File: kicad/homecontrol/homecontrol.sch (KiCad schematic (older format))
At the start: 71 parts, among them J1 Screw_Terminal_01x09, J2 Screw_Terminal_01x09, J3 Screw_Terminal_01x09, J4 Screw_Terminal_01x09, J5 AVR-ISP-10, U1 ATmega48P-20PU, U2 L7805ABP, U3 ULN2803A, U4 MAX232EEPE+, U5 A817, U6 A817

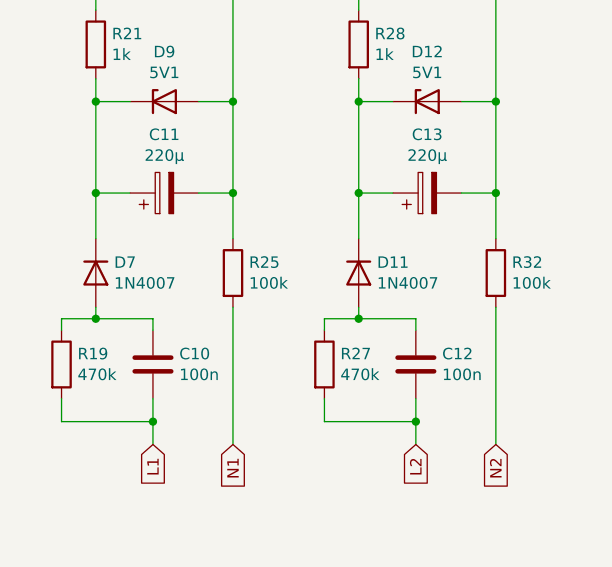
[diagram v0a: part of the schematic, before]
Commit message: Updated footprints and BOM
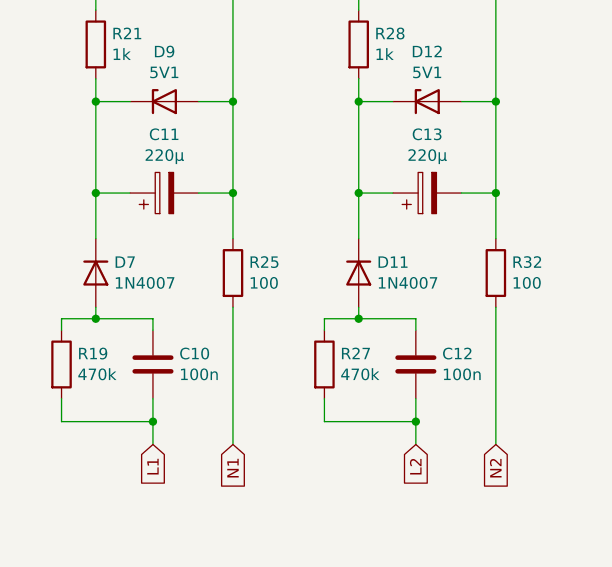
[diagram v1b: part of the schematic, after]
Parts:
- C1, C4: footprint Capacitor_THT:C_Disc_D6.0mm_W2.5mm_P5.00mm -> Capacitor_THT:C_Rect_L7.0mm_W2.5mm_P5.00mm; Supplier (none) -> Digikey; Supplier_Ref (none) -> BC1101CT-ND; Voltage 16V -> 50V
- C10: footprint Capacitor_THT:C_Rect_L10.3mm_W4.5mm_P7.50mm_MKS4 -> Capacitor_THT:C_Rect_L13.0mm_W4.0mm_P10.00mm_FKS3_FKP3_MKS4
- C11, C13: footprint Capacitor_THT:CP_Radial_D10.0mm_P3.50mm -> Capacitor_THT:CP_Radial_D6.3mm_P2.50mm; Supplier (none) -> Digikey; Supplier_Ref (none) -> P14393-ND
- C12: footprint Capacitor_THT:C_Rect_L10.3mm_W5.0mm_P7.50mm_MKS4 -> Capacitor_THT:C_Rect_L13.0mm_W4.0mm_P10.00mm_FKS3_FKP3_MKS4
- C2: footprint Capacitor_THT:C_Disc_D6.0mm_W2.5mm_P5.00mm -> Capacitor_THT:C_Disc_D4.7mm_W2.5mm_P5.00mm; Supplier (none) -> Digikey; Supplier_Ref (none) -> 445-173597-1-ND
- C3: footprint Capacitor_THT:CP_Radial_D10.0mm_P3.50mm -> Capacitor_THT:CP_Radial_D6.3mm_P2.50mm; Type MLCC -> (none)
- C5, C6, C7, C8, C9: footprint Capacitor_THT:C_Disc_D6.0mm_W2.5mm_P5.00mm -> Capacitor_THT:C_Rect_L4.6mm_W3.0mm_P2.50mm_MKS02_FKP02; Supplier (none) -> Digikey; Supplier_Ref (none) -> 445-173138-1-ND
- D1: footprint Diode_THT:D_DO-41_SOD81_P10.16mm_Horizontal -> Diode_THT:D_DO-35_SOD27_P2.54mm_Vertical_KathodeUp
- D10, D13, D2, D3, D4, D5, D6, D8: footprint Diode_THT:D_A-405_P2.54mm_Vertical_KathodeUp -> Diode_THT:D_DO-35_SOD27_P2.54mm_Vertical_KathodeUp; Power (none) -> 400mW; Supplier (none) -> Digikey; Supplier_Ref (none) -> 1727-1864-1-ND
- D12, D9: footprint Diode_THT:D_A-405_P2.54mm_Vertical_KathodeUp -> Diode_THT:D_DO-35_SOD27_P2.54mm_Vertical_KathodeUp
- R1, R10, R11, R12, R13, R14, R15, R16, R17, R18, R2, R20, R21, R22, R23, R24, R26, R28, R29, R3, R30, R31, R33, R4, R5, R6, R7, R8, R9: footprint Resistor_THT:R_Axial_DIN0204_L3.6mm_D1.6mm_P2.54mm_Vertical -> Resistor_THT:R_Axial_DIN0207_L6.3mm_D2.5mm_P2.54mm_Vertical
- R19, R27: footprint Resistor_THT:R_Axial_DIN0204_L3.6mm_D1.6mm_P2.54mm_Vertical -> Resistor_THT:R_Axial_DIN0207_L6.3mm_D2.5mm_P10.16mm_Horizontal
- R25, R32: value 100k -> 100; footprint Resistor_THT:R_Axial_DIN0204_L3.6mm_D1.6mm_P2.54mm_Vertical -> Resistor_THT:R_Axial_DIN0207_L6.3mm_D2.5mm_P10.16mm_Horizontal
- U1: footprint Package_DIP:DIP-28_W7.62mm -> Package_DIP:DIP-28_W7.62mm_Socket
- U2: Supplier (none) -> Digikey; Supplier_Ref (none) -> 497-4226-5-ND
- U3: footprint Package_DIP:DIP-18_W7.62mm -> Package_DIP:DIP-18_W7.62mm_Socket; Supplier (none) -> Digikey; Supplier_Ref (none) -> 497-2356-5-ND
- U4: Supplier (none) -> Digikey; Supplier_Ref (none) -> MAX232EEPE+-ND

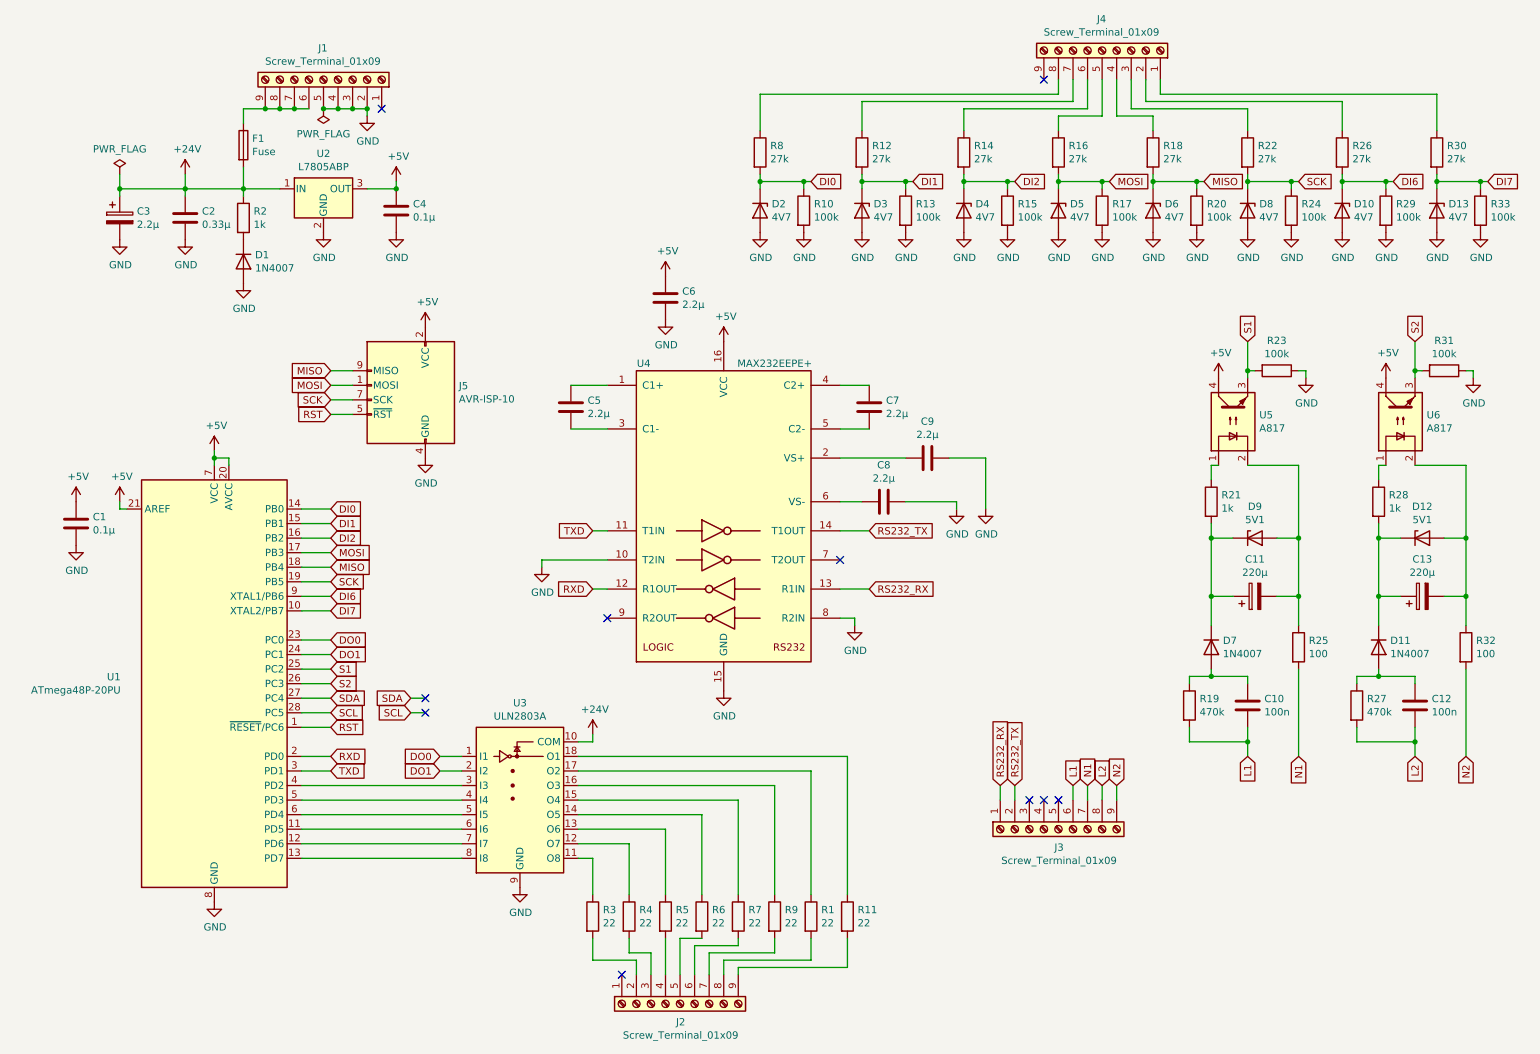
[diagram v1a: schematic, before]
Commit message: First full PCB layout of HomeControl
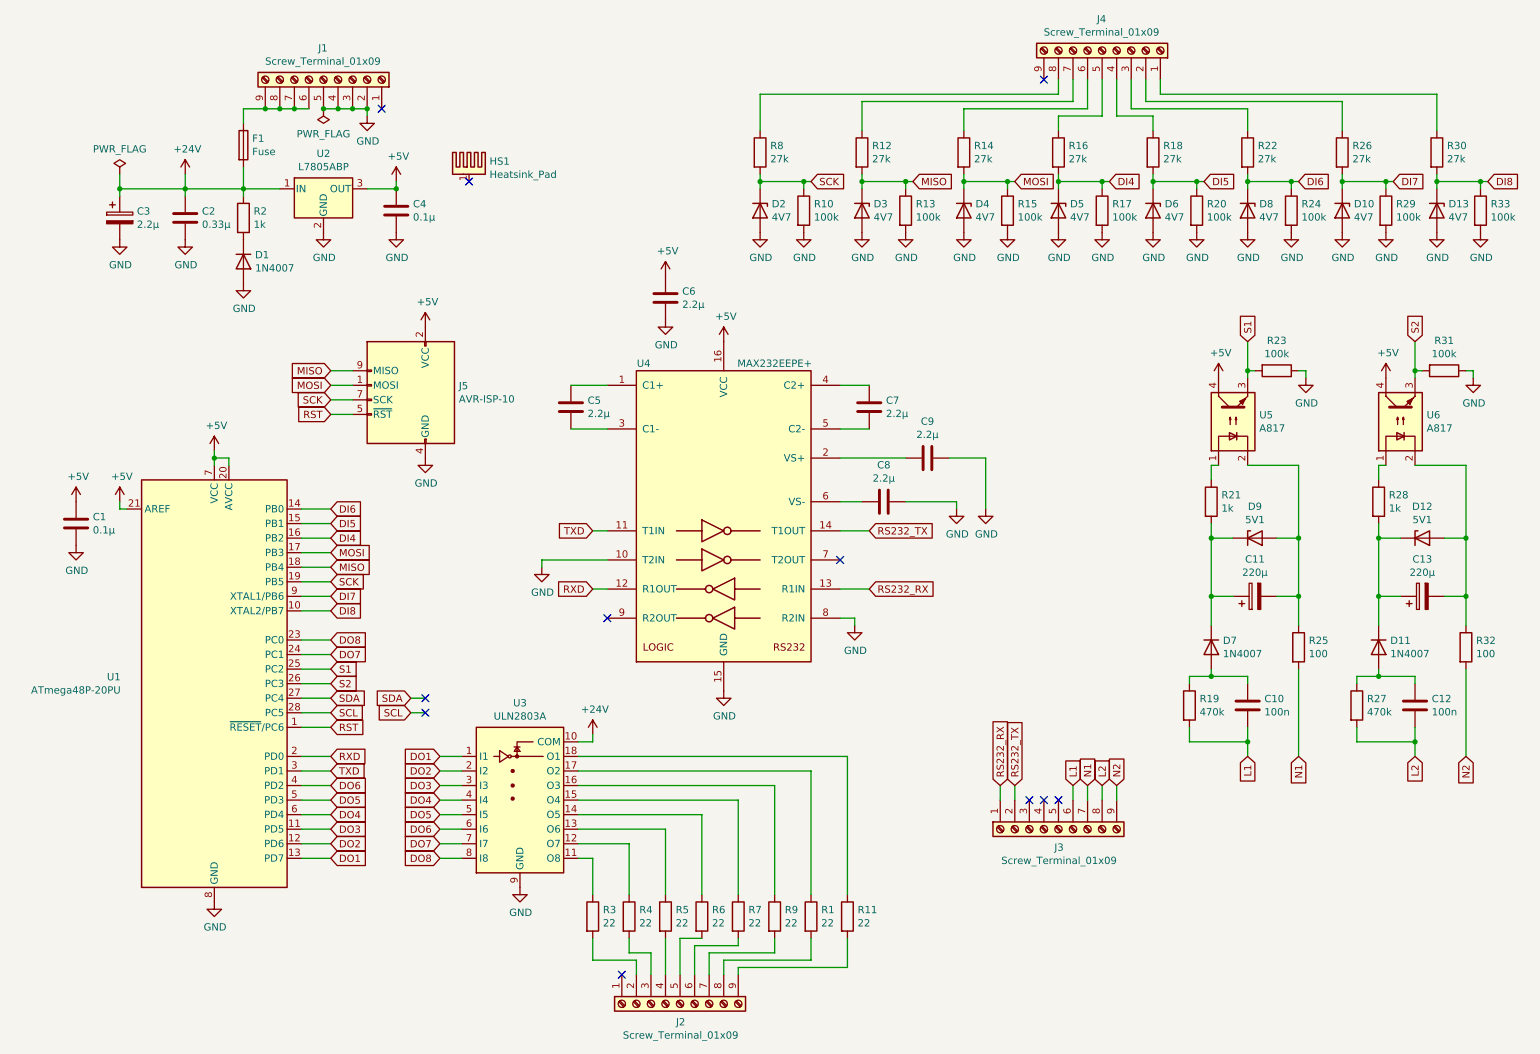
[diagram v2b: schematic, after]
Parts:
- added HS1: Heatsink_Pad, Custom_Library:Heatsink_Aavid_TO-220_H12.7mm, symbol Mechanical:Heatsink_Pad
- J5: footprint Connector_PinHeader_2.54mm:PinHeader_2x05_P2.54mm_Vertical -> Connector_IDC:IDC-Header_2x05_P2.54mm_Vertical
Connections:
- net DI6: now also D8.1 (K), R22.2, R24.1, U1.14 (PB0); no longer D10.1 (K), R26.2, R29.1, U1.9 (XTAL1/PB6)
- net DI7: now also D10.1 (K), R26.2, R29.1, U1.9 (XTAL1/PB6); no longer D13.1 (K), R30.2, R33.1, U1.10 (XTAL2/PB7)
- net DO1: now also U1.13 (PD7), U3.1 (I1); no longer U1.24 (PC1), U3.2 (I2)
- net MISO: now also D3.1 (K), R12.2, R13.1; no longer D6.1 (K), R18.2, R20.1
- net MOSI: now also D4.1 (K), R14.2, R15.1; no longer D5.1 (K), R16.2, R17.1
- net SCK: now also D2.1 (K), R10.1, R8.2; no longer D8.1 (K), R22.2, R24.1
- net DO3: now reaches U1.11 (PD5)
- net DO3: now also U3.3 (I3); no longer U3.6 (I6)
- net DO2: now reaches U1.12 (PD6)
- net DO2: now also U3.2 (I2); no longer U3.7 (I7)
- net DO8: now reaches U3.8 (I8)
- net DO8: now also U1.23 (PC0); no longer U1.13 (PD7)
- net DO6: now reaches U1.4 (PD2)
- net DO6: now also U3.6 (I6); no longer U3.3 (I3)
- net DO4: now reaches U3.4 (I4)
- net DO4: now also U1.6 (PD4); no longer U1.5 (PD3)
- net DO5: now reaches U3.5 (I5)
- net DO5: now also U1.5 (PD3); no longer U1.6 (PD4)
- removed net DI0: D2.1 (K), R10.1, R8.2, U1.14 (PB0)
- removed net DI1: D3.1 (K), R12.2, R13.1, U1.15 (PB1)
- removed net DI2: D4.1 (K), R14.2, R15.1, U1.16 (PB2)
- removed net DO0: U1.23 (PC0), U3.1 (I1)
- new net DI4: D5.1 (K), R16.2, R17.1, U1.16 (PB2)
- new net DI5: D6.1 (K), R18.2, R20.1, U1.15 (PB1)
- new net DI8: D13.1 (K), R30.2, R33.1, U1.10 (XTAL2/PB7)
- new net DO7: U1.24 (PC1), U3.7 (I7)
- no-connect marks 10 -> 11
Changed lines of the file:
@@
-$EndComp
-$Comp
-L Interface_UART:MAX232 U4
-U 1 1 609E0879
-P 5550 4050
-F 0 "U4" H 5000 5100 50  0000 C CNN
-F 1 "MAX232EEPE+" H 5900 5100 50  0000 C CNN
-F 2 "Package_DIP:DIP-16_W7.62mm_Socket" H 5600 3000 50  0001 L CNN
-F 3 "https://datasheets.maximintegrated.com/en/ds/MAX202E-MAX241E.pdf" H 5550 4150 50  0001 C CNN
-F 4 "Digikey" H 5550 4050 50  0001 C CNN "Supplier"
-F 5 "MAX232EEPE+-ND" H 5550 4050 50  0001 C CNN "Supplier_Ref"
-	1    5550 4050
-	1    0    0    -1
 $EndComp
 $Comp
@@
 F 0 "J5" H 3070 3346 50  0000 R CNN
 F 1 "AVR-ISP-10" H 3070 3255 50  0000 R CNN
-F 2 "Connector_PinHeader_2.54mm:PinHeader_2x05_P2.54mm_Vertical" V 3150 3300 50  0001 C CNN
+F 2 "Connector_IDC:IDC-Header_2x05_P2.54mm_Vertical" V 3150 3300 50  0001 C CNN
 F 3 " ~" H 2125 2700 50  0001 C CNN
 	1    3400 3250
@@
 Text GLabel 2850 5800 2    50   Input ~ 0
 TXD
-Text GLabel 4650 4550 0    50   Input ~ 0
-RXD
-Text GLabel 4650 4150 0    50   Input ~ 0
-TXD
-Wire Wire Line
-	4650 4150 4750 4150
-Wire Wire Line
-	4750 4550 4650 4550
 Wire Wire Line
 	2850 5700 2650 5700
@@
 SDA
 Text GLabel 2850 4000 2    50   Input ~ 0
-DI0
+DI6
 Text GLabel 2850 4100 2    50   Input ~ 0
-DI1
+DI5
 Text GLabel 2850 4200 2    50   Input ~ 0
-DI2
+DI4
 Text GLabel 2850 4600 2    50   Input ~ 0
-DI6
+DI7
 Text GLabel 2850 4700 2    50   Input ~ 0
-DI7
+DI8
 Wire Wire Line
 	2850 4700 2650 4700
@@
 	2850 4000 2650 4000
 Text GLabel 2850 4900 2    50   Input ~ 0
-DO0
+DO8
 Text GLabel 2850 5000 2    50   Input ~ 0
-DO1
+DO7
 Wire Wire Line
 	2850 4900 2650 4900
 Wire Wire Line
 	2650 5000 2850 5000
-Wire Wire Line
-	2650 5900 3750 5900
-Wire Wire Line
-	2650 6000 3750 6000
-Wire Wire Line
-	2650 6100 3750 6100
-Wire Wire Line
-	2650 6200 3750 6200
-Wire Wire Line
-	2650 6300 3750 6300
-Wire Wire Line
-	2650 6400 3750 6400
 $Comp
 L power:GND #PWR010
@@
 Wire Wire Line
 	4650 5600 4550 5600
+Text GLabel 3600 6400 0    50   Input ~ 0
+DO8
 Text GLabel 3600 5700 0    50   Input ~ 0
-DO0
-Text GLabel 3600 5800 0    50   Input ~ 0
 DO1
 Wire Wire Line
@@
 	1    0    0    -1
 $EndComp
-$Comp
-L power:GND #PWR012
-U 1 1 60B23C16
-P 4300 4400
-F 0 "#PWR012" H 4300 4150 50  0001 C CNN
-F 1 "GND" H 4305 4227 50  0000 C CNN
-F 2 "" H 4300 4400 50  0001 C CNN
-F 3 "" H 4300 4400 50  0001 C CNN
-	1    4300 4400
-	1    0    0    -1
-$EndComp
-Wire Wire Line
-	4300 4400 4300 4350
-Wire Wire Line
-	4300 4350 4750 4350
-$Comp
-L power:GND #PWR015
-U 1 1 60B25DE9
-P 6450 4800
-F 0 "#PWR015" H 6450 4550 50  0001 C CNN
-F 1 "GND" H 6455 4627 50  0000 C CNN
-F 2 "" H 6450 4800 50  0001 C CNN
-F 3 "" H 6450 4800 50  0001 C CNN
-	1    6450 4800
-	1    0    0    -1
-$EndComp
-Wire Wire Line
-	6450 4800 6450 4750
-Wire Wire Line
-	6450 4750 6350 4750
-Text GLabel 6550 4550 2    50   Input ~ 0
-RS232_RX
-Text GLabel 6550 4150 2    50   Input ~ 0
-RS232_TX
-Wire Wire Line
-	6350 4150 6550 4150
-Wire Wire Line
-	6550 4550 6350 4550
 Text GLabel 7450 5900 1    50   Input ~ 0
 RS232_RX
@@
 $EndComp
 Text GLabel 6850 1750 2    50   Input ~ 0
-DI1
+MISO
 Wire Wire Line
 	6800 1750 6850 1750
@@
 $EndComp
 Text GLabel 6150 1750 2    50   Input ~ 0
-DI0
+SCK
 Wire Wire Line
 	6100 1750 6150 1750
@@
 $EndComp
 Text GLabel 7550 1750 2    50   Input ~ 0
-DI2
+MOSI
 Wire Wire Line
 	7500 1750 7550 1750
@@
 $EndComp
 Text GLabel 8200 1750 2    50   Input ~ 0
-MOSI
+DI4
 Wire Wire Line
 	8150 1750 8200 1750
@@
 $EndComp
 Text GLabel 8850 1750 2    50   Input ~ 0
-MISO
+DI5
 Wire Wire Line
 	8800 1750 8850 1750
@@
 $EndComp
 Text GLabel 9500 1750 2    50   Input ~ 0
-SCK
+DI6
 Wire Wire Line
 	9450 1750 9500 1750
@@
 $EndComp
 Text GLabel 10150 1750 2    50   Input ~ 0
-DI6
+DI7
 Wire Wire Line
 	10100 1750 10150 1750
@@
 $EndComp
 Text GLabel 10800 1750 2    50   Input ~ 0
-DI7
+DI8
 Wire Wire Line
 	10750 1750 10800 1750
@@
 	2850 5400 2650 5400
 NoConn ~ 7750 6000
-NoConn ~ 6350 4350
-NoConn ~ 4750 4750
 Text GLabel 3400 5300 0    50   Input ~ 0
 SDA
@@
 L1
 NoConn ~ 7850 6000
+$Comp
+L Interface_UART:MAX232 U4
+U 1 1 609E0879
+P 5550 4050
+F 0 "U4" H 5000 5100 50  0000 C CNN
+F 1 "MAX232EEPE+" H 5900 5100 50  0000 C CNN
+F 2 "Package_DIP:DIP-16_W7.62mm_Socket" H 5600 3000 50  0001 L CNN
+F 3 "https://datasheets.maximintegrated.com/en/ds/MAX202E-MAX241E.pdf" H 5550 4150 50  0001 C CNN
+F 4 "Digikey" H 5550 4050 50  0001 C CNN "Supplier"
+F 5 "MAX232EEPE+-ND" H 5550 4050 50  0001 C CNN "Supplier_Ref"
+	1    5550 4050
+	1    0    0    -1
+$EndComp
+Text GLabel 6550 4550 2    50   Input ~ 0
+RS232_RX
+Text GLabel 6550 4150 2    50   Input ~ 0
+RS232_TX
+NoConn ~ 6350 4350
+Wire Wire Line
+	6350 4150 6550 4150
+Wire Wire Line
+	6550 4550 6350 4550
+Wire Wire Line
+	6450 4800 6450 4750
+Wire Wire Line
+	6450 4750 6350 4750
+$Comp
+L power:GND #PWR015
+U 1 1 60B25DE9
+P 6450 4800
+F 0 "#PWR015" H 6450 4550 50  0001 C CNN
+F 1 "GND" H 6455 4627 50  0000 C CNN
+F 2 "" H 6450 4800 50  0001 C CNN
+F 3 "" H 6450 4800 50  0001 C CNN
+	1    6450 4800
+	1    0    0    -1
+$EndComp
+$Comp
+L power:GND #PWR012
+U 1 1 60B23C16
+P 4300 4400
+F 0 "#PWR012" H 4300 4150 50  0001 C CNN
+F 1 "GND" H 4305 4227 50  0000 C CNN
+F 2 "" H 4300 4400 50  0001 C CNN
+F 3 "" H 4300 4400 50  0001 C CNN
+	1    4300 4400
+	1    0    0    -1
+$EndComp
+Wire Wire Line
+	4300 4400 4300 4350
+Text GLabel 4650 4150 0    50   Input ~ 0
+TXD
+Wire Wire Line
+	4650 4150 4750 4150
+NoConn ~ 4750 4750
+Wire Wire Line
+	4750 4550 4650 4550
+Wire Wire Line
+	4300 4350 4750 4350
+Text GLabel 4650 4550 0    50   Input ~ 0
+RXD
+Text GLabel 3600 5800 0    50   Input ~ 0
+DO2
+Text GLabel 3600 5900 0    50   Input ~ 0
+DO3
+Text GLabel 3600 6000 0    50   Input ~ 0
+DO4
+Text GLabel 3600 6100 0    50   Input ~ 0
+DO5
+Text GLabel 3600 6200 0    50   Input ~ 0
+DO6
+Text GLabel 3600 6300 0    50   Input ~ 0
+DO7
+Text GLabel 2850 5900 2    50   Input ~ 0
+DO6
+Text GLabel 2850 6000 2    50   Input ~ 0
+DO5
+Text GLabel 2850 6100 2    50   Input ~ 0
+DO4
+Text GLabel 2850 6200 2    50   Input ~ 0
+DO3
+Text GLabel 2850 6300 2    50   Input ~ 0
+DO2
+Text GLabel 2850 6400 2    50   Input ~ 0
+DO1
+Wire Wire Line
+	2650 5900 2850 5900
+Wire Wire Line
+	2850 6000 2650 6000
+Wire Wire Line
+	2650 6100 2850 6100
+Wire Wire Line
+	2850 6200 2650 6200
+Wire Wire Line
+	2650 6300 2850 6300
+Wire Wire Line
+	2850 6400 2650 6400
+Wire Wire Line
+	3600 5900 3750 5900
+Wire Wire Line
+	3750 6000 3600 6000
+Wire Wire Line
+	3600 6100 3750 6100
+Wire Wire Line
+	3750 6200 3600 6200
+Wire Wire Line
+	3600 6300 3750 6300
+Wire Wire Line
+	3750 6400 3600 6400
+$Comp
+L Mechanical:Heatsink_Pad HS1
+U 1 1 61C9F3A7
+P 3800 1650
+F 0 "HS1" H 3941 1689 50  0000 L CNN
+F 1 "Heatsink_Pad" H 3941 1598 50  0000 L CNN
+F 2 "Custom_Library:Heatsink_Aavid_TO-220_H12.7mm" H 3812 1600 50  0001 C CNN
+F 3 "~" H 3812 1600 50  0001 C CNN
+	1    3800 1650
+	1    0    0    -1
+$EndComp
+NoConn ~ 3800 1750
 $EndSCHEMATC
